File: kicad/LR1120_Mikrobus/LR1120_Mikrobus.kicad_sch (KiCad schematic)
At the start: 110 parts, among them CON1 MIKROBUS_MODULE_CONN, J1 Conn_01x07, J2 Conn_01x07, Q1 NX2016SA-32M-EXS00A-CS06465, Q2 NT2016SA-32M-END4263A, Q3 NX3215SA, U1 LR1120, U2 SKY13588-460LF, U5 LIS2DE12, U7 M24128-BFMH6TG, U8 BGA524N6E6327XTSA1

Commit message: more components placed
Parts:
- removed uBUS_connector1: MIKROE-924, Mikrobus:MIKROBUS_MODULE_CONN, symbol MIKROE-924:MIKROE-924
- C53: footprint Capacitor_SMD:C_0201_0603Metric -> Capacitor_SMD:C_0402_1005Metric
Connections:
- net GND: now also Q2.3 (GND), Q2.4 (GND); no longer Q2.1 (GND), Q2.2 (GND), R3.1
- net XTA: now also R3.1; no longer C50.1, R3.2
- net at C50.2: now also Q2.2 (OUT); no longer Q2.3 (OUT)
- net at C49.1, FB1.2: now also Q2.1 (VCC); no longer Q2.4 (VCC)
- new net: C50.1, R3.2
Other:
- moved on the sheet: R3
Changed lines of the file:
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@@
   (junction (at 214.63 62.23) (diameter 0) (color 0 0 0 0)
   )
-  (junction (at 386.08 228.6) (diameter 0) (color 0 0 0 0)
-  )
   (junction (at 203.2 165.1) (diameter 0) (color 0 0 0 0)
   )
@@
     (stroke (width 0) (type default) (color 0 0 0 0))
   )
-  (wire (pts (xy 386.08 228.6) (xy 388.62 228.6))
-    (stroke (width 0) (type default) (color 0 0 0 0))
-  )
   (wire (pts (xy 210.82 265.43) (xy 209.55 265.43))
     (stroke (width 0) (type default) (color 0 0 0 0))
@@
     (stroke (width 0) (type default) (color 0 0 0 0))
   )
-  (wire (pts (xy 382.27 228.6) (xy 386.08 228.6))
-    (stroke (width 0) (type default) (color 0 0 0 0))
-  )
   (wire (pts (xy 123.19 109.22) (xy 123.19 111.76))
     (stroke (width 0) (type default) (color 0 0 0 0))
@@
     (stroke (width 0) (type default) (color 0 0 0 0))
   )
+  (wire (pts (xy 382.27 228.6) (xy 384.81 228.6))
+    (stroke (width 0) (type default) (color 0 0 0 0))
+  )
   (wire (pts (xy 93.98 247.65) (xy 93.98 240.03))
     (stroke (width 0) (type default) (color 0 0 0 0))
@@
     (stroke (width 0) (type default) (color 0 0 0 0))
   )
-  (wire (pts (xy 386.08 228.6) (xy 386.1308 231.0892))
-    (stroke (width 0) (type default) (color 0 0 0 0))
-  )
   (wire (pts (xy 356.87 189.23) (xy 353.06 189.23))
     (stroke (width 0) (type default) (color 0 0 0 0))
@@
     (stroke (width 0) (type default) (color 0 0 0 0))
   )
+  (wire (pts (xy 392.43 228.6) (xy 394.97 228.6))
+    (stroke (width 0) (type default) (color 0 0 0 0))
+  )
   (wire (pts (xy 190.5 273.05) (xy 193.04 273.05))
     (stroke (width 0) (type default) (color 0 0 0 0))
@@
     (effects (font (size 1.27 1.27)) (justify left bottom))
   )
-  (label "XTA" (at 388.62 228.6 0)
+  (label "XTA" (at 394.97 228.6 0)
     (effects (font (size 1.27 1.27)) (justify left bottom))
   )
@@
     (property "Reference" "C58" (id 0) (at 238.76 35.56 0))
     (property "Value" "1nF" (id 1) (at 237.49 38.1 0))
-    (property "Footprint" "Capacitor_SMD:C_0201_0603Metric" (id 2) (at 240.03 57.15 90))
+    (property "Footprint" "Capacitor_SMD:C_0201_0603Metric" (id 2) (at 240.03 57.15 90)
+      (effects (font (size 1.27 1.27)) hide)
+    )
     (property "Datasheet" "~" (id 3) (at 242.57 38.1 0)
       (effects (font (size 1.27 1.27)) hide)
@@
     (property "Reference" "C53" (id 0) (at 298.45 74.93 0))
     (property "Value" "NC" (id 1) (at 297.18 77.47 0))
-    (property "Footprint" "Capacitor_SMD:C_0201_0603Metric" (id 2) (at 301.2948 73.66 0)
+    (property "Footprint" "Capacitor_SMD:C_0402_1005Metric" (id 2) (at 301.2948 73.66 0)
       (effects (font (size 1.27 1.27)) hide)
     )
@@
     (pin "2")
   )
-  (symbol (lib_id "MIKROE-924:MIKROE-924") (at 259.08 177.8 0) (unit 1)
-    (in_bom yes) (on_board yes)
-    (property "Reference" "uBUS_connector1" (id 0) (at 274.32 170.18 0))
-    (property "Value" "MIKROE-924" (id 1) (at 274.32 172.72 0))
-    (property "Footprint" "Mikrobus:MIKROBUS_MODULE_CONN" (id 2) (at 285.75 175.26 0)
-      (effects (font (size 1.27 1.27)) (justify left) hide)
-    )
-    (property "Datasheet" "https://www.mikroe.com/microsd-click" (id 3) (at 285.75 177.8 0)
-      (effects (font (size 1.27 1.27)) (justify left) hide)
-    )
-    (property "Description" "microSD click mikroBUS" (id 4) (at 285.75 180.34 0)
-      (effects (font (size 1.27 1.27)) (justify left) hide)
-    )
-    (property "Height" "5" (id 5) (at 285.75 182.88 0)
-      (effects (font (size 1.27 1.27)) (justify left) hide)
-    )
-    (property "Manufacturer_Name" "MIKROELEKTRONIKA" (id 6) (at 285.75 185.42 0)
-      (effects (font (size 1.27 1.27)) (justify left) hide)
-    )
-    (property "Manufacturer_Part_Number" "MIKROE-924" (id 7) (at 285.75 187.96 0)
-      (effects (font (size 1.27 1.27)) (justify left) hide)
-    )
-    (property "Mouser Part Number" "932-MIKROE-924" (id 8) (at 285.75 190.5 0)
-      (effects (font (size 1.27 1.27)) (justify left) hide)
-    )
-    (property "Mouser Price/Stock" "https://www.mouser.com/Search/Refine.aspx?Keyword=932-MIKROE-924" (id 9) (at 285.75 193.04 0)
-      (effects (font (size 1.27 1.27)) (justify left) hide)
-    )
-    (property "Arrow Part Number" "" (id 10) (at 285.75 195.58 0)
-      (effects (font (size 1.27 1.27)) (justify left) hide)
-    )
-    (property "Arrow Price/Stock" "" (id 11) (at 285.75 198.12 0)
-      (effects (font (size 1.27 1.27)) (justify left) hide)
-    )
-    (pin "1")
-    (pin "10")
-    (pin "11")
-    (pin "12")
-    (pin "13")
-    (pin "14")
-    (pin "15")
-    (pin "16")
-    (pin "2")
-    (pin "3")
-    (pin "4")
-    (pin "5")
-    (pin "6")
-    (pin "7")
-    (pin "8")
-    (pin "9")
-  )
   (symbol (lib_id "Device:R") (at 199.39 182.88 0) (unit 1)
     (in_bom yes) (on_board yes) (fields_autoplaced)
@@
     (pin "2")
   )
-  (symbol (lib_id "Device:R") (at 386.1308 234.8992 180) (unit 1)
+  (symbol (lib_id "Device:R") (at 388.62 228.6 270) (unit 1)
     (in_bom yes) (on_board yes)
-    (property "Reference" "R3" (id 0) (at 383.2352 234.95 0))
-    (property "Value" "220" (id 1) (at 389.6868 235.204 0))
-    (property "Footprint" "Resistor_SMD:R_0201_0603Metric" (id 2) (at 387.9088 234.8992 90)
+    (property "Reference" "R3" (id 0) (at 388.6708 231.4956 90))
+    (property "Value" "220" (id 1) (at 388.9248 225.044 90))
+    (property "Footprint" "Resistor_SMD:R_0201_0603Metric" (id 2) (at 388.62 226.822 90)
       (effects (font (size 1.27 1.27)) hide)
     )
-    (property "Datasheet" "~" (id 3) (at 386.1308 234.8992 0)
+    (property "Datasheet" "~" (id 3) (at 388.62 228.6 0)
       (effects (font (size 1.27 1.27)) hide)
     )
@@
       (effects (font (size 1.27 1.27)) hide)
     )
-    (pin "1")
-    (pin "2")
     (pin "3")
     (pin "4")
+    (pin "2")
+    (pin "1")
   )
   (symbol (lib_id "power:GND") (at 242.57 276.86 0) (mirror y) (unit 1)
@@
     (pin "2")
   )
-  (symbol (lib_id "power:GND") (at 386.08 238.76 0) (unit 1)
-    (in_bom yes) (on_board yes)
-    (property "Reference" "#PWR0145" (id 0) (at 386.08 245.11 0)
-      (effects (font (size 1.27 1.27)) hide)
-    )
-    (property "Value" "GND" (id 1) (at 386.08 242.57 0))
-    (property "Footprint" "" (id 2) (at 386.08 238.76 0)
-      (effects (font (size 1.27 1.27)) hide)
-    )
-    (property "Datasheet" "" (id 3) (at 386.08 238.76 0)
-      (effects (font (size 1.27 1.27)) hide)
-    )
-    (pin "1")
-  )
   (symbol (lib_id "Device:C") (at 123.19 115.57 0) (unit 1)
     (in_bom yes) (on_board yes) (fields_autoplaced)
@@
       (reference "#PWR0144") (unit 1) (value "GND") (footprint "")
     )
-    (path "/9ceef2a2-12cb-47bc-9f3b-12460f70dbc2"
-      (reference "#PWR0145") (unit 1) (value "GND") (footprint "")
-    )
     (path "/63c4f417-7c3d-4a88-9920-5a800c296035"
       (reference "#PWR0146") (unit 1) (value "GND") (footprint "")
@@
     )
     (path "/20924966-d251-4062-bd99-6a0a4e9003bc"
-      (reference "C53") (unit 1) (value "NC") (footprint "Capacitor_SMD:C_0201_0603Metric")
+      (reference "C53") (unit 1) (value "NC") (footprint "Capacitor_SMD:C_0402_1005Metric")
     )
     (path "/3dcf9ad7-bb51-4c2b-9863-3c3a199a22b4"
@@
       (reference "VDD_RF_SW1") (unit 1) (value "Jumper_2_Bridged") (footprint "Connector_PinHeader_2.54mm:PinHeader_1x02_P2.54mm_Vertical")
     )
-    (path "/30d9f59d-f72b-41c4-8214-d95fedfe532c"
-      (reference "uBUS_connector1") (unit 1) (value "MIKROE-924") (footprint "Mikrobus:MIKROBUS_MODULE_CONN")
-    )
   )

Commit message: All components placed
Last step: routing
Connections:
- net VDD_3V3: now also C52.1, U7.1 (VCC)
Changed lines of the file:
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@@
   (junction (at 215.9 189.23) (diameter 0) (color 0 0 0 0)
   )
+  (junction (at 339.09 127) (diameter 0) (color 0 0 0 0)
+  )
   (junction (at 251.46 88.9) (diameter 0) (color 0 0 0 0)
   )
@@
   )
   (wire (pts (xy 132.08 119.38) (xy 132.08 120.65))
+    (stroke (width 0) (type default) (color 0 0 0 0))
+  )
+  (wire (pts (xy 335.28 127) (xy 339.09 127))
     (stroke (width 0) (type default) (color 0 0 0 0))
   )
@@
     (effects (font (size 1.27 1.27)) (justify right bottom))
   )
+  (label "VDD_3V3" (at 335.28 127 180)
+    (effects (font (size 1.27 1.27)) (justify right bottom))
+  )

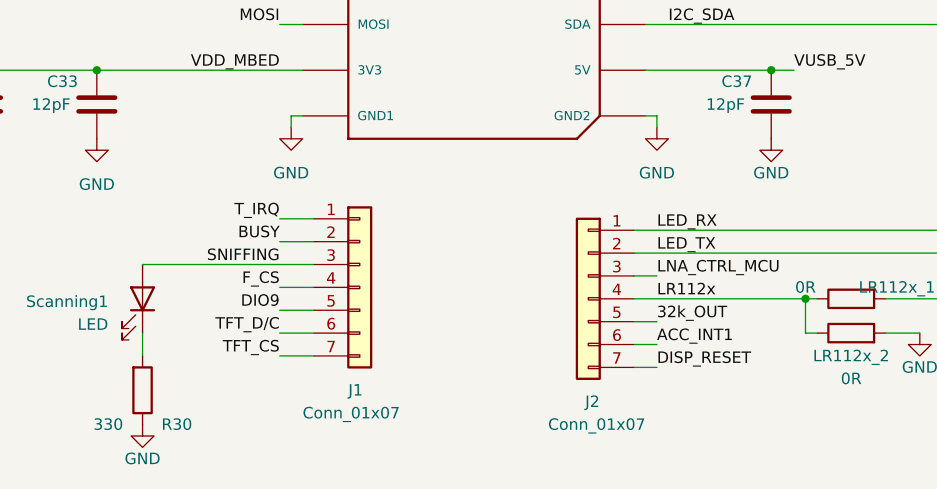
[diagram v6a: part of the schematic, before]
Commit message: all routes traced. ground planes set.
All routes were traced, The ground planes were set with the appropriate cut out for the crystal oscillators.
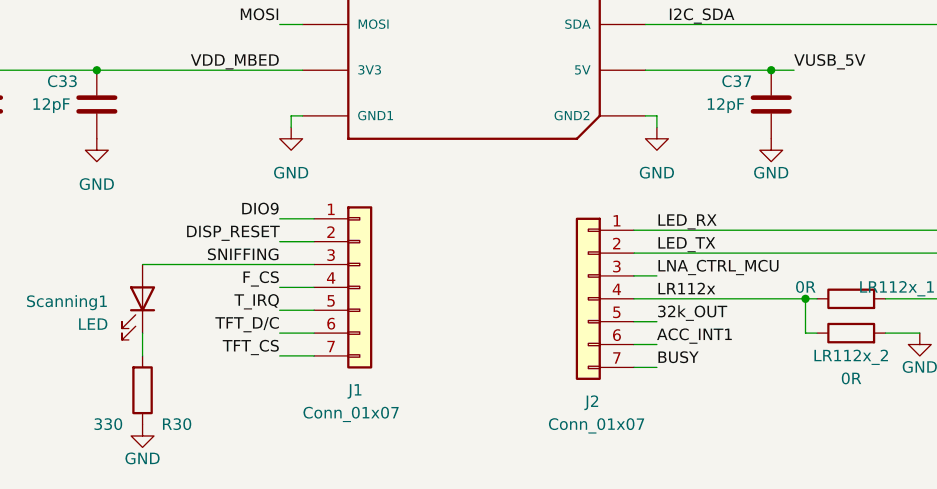
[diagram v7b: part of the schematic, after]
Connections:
- net BUSY: now also J2.7 (Pin_7); no longer J1.2 (Pin_2)
- net DIO9: now also J1.1 (Pin_1); no longer J1.5 (Pin_5)
- net DISP_RESET: now also J1.2 (Pin_2); no longer J2.7 (Pin_7)
- net T_IRQ: now also J1.5 (Pin_5); no longer J1.1 (Pin_1)

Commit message: pcb design guideline checked
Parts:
- C10, C15, C21: value 12pF -> 47pF
- C12: value 0.5pF -> 1.8pF
- C13: value NC -> 3pF
- C17: value 0.5pF -> 1.5pF
- C18: value 1pF -> 1.2pF
- C31, C32: value 0.5pF -> 3.3pF
- C33: value 12pF -> 100nF
- C34, C35, C37: value 12pF -> 1uF
- C38: value 12pF -> 10uF
- C39: value 1.5pF -> 1nF
- C47: value 1pF -> 100nF
- C48: value 1pF -> 4.7uF
- C49: value 0.5pF -> 100nF
- C50: value 1pF -> 10pF
- C52: value NC -> NC (100nF)
- C54: value 33pF -> 1nF
- C55: value 0.5pF -> 470pF
- C8: value NC -> 1.2pF
- C9: value 0.5pF -> 6.8pF
- FB1: value FerriteBead -> 10R (100MHz)
- L10: value 33nH -> 47nH
- L14: value 33nH -> 8.2nH
- L17: value 9.5nH -> 9.1nH
- L3, L4: value 9.5nH -> 47nH
- L5: value 9.5nH -> 3.3nH
- L6: value 9.5nH -> 8.2nH
- L7: value 9.5nH -> 2.7nH
- L8: value 9.5nH -> 6.8nH
- L9: value 9.5nH -> 22nH
- LR112x_1: value 0R -> 10k
- R31: value NC -> NC (10k)
- R33: value R -> 200R
- R5, R6: value NC -> NC (4.7k)
- R8: value 0R -> 100R
